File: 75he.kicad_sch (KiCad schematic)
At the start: 0 parts

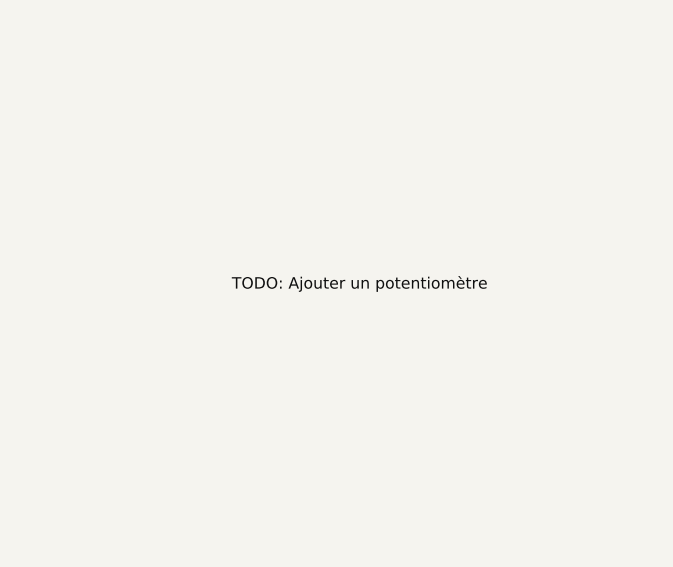
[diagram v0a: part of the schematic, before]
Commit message: Add rotary encoder symbol;
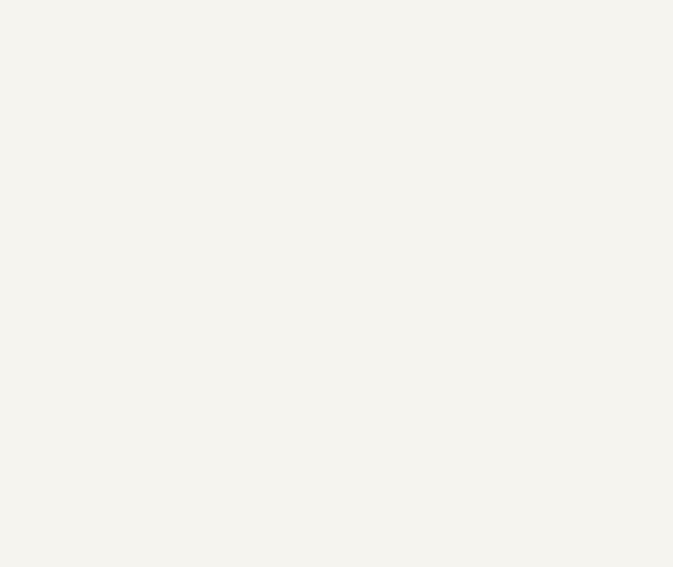
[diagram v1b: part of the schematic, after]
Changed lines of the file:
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@@
-		)
-	)
-	(label "TODO: Ajouter un potentiomètre"
-		(at 231.14 119.38 0)
-		(effects
-			(font
-				(size 1.27 1.27)
-			)
-			(justify left bottom)
 		)
 	)

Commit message: fixes & doc
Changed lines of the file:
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@@
+		)
+	)
+	(label "TODO: Ajouter un potentiomètre"
+		(at 231.14 119.38 0)
+		(effects
+			(font
+				(size 1.27 1.27)
+			)
+			(justify left bottom)
 		)
 	)
